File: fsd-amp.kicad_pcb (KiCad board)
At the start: 2 copper layers, 13 parts, among them J1001 Screw_Terminal_01x06, J1004 AudioJack2_Ground_Switch, Q1001 FZT 653 ZET, Q1002 FZT 653 ZET, Q1003 FZT 753 ZET

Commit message: define edge cuts board outline
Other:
- board outline added: 100 x 75 mm
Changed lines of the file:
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@@
 		)
 	)
+	(gr_rect
+		(start 100 50)
+		(end 200 125)
+		(stroke
+			(width 0.05)
+			(type default)
+		)
+		(fill none)
+		(layer "Edge.Cuts")
+	)
 )

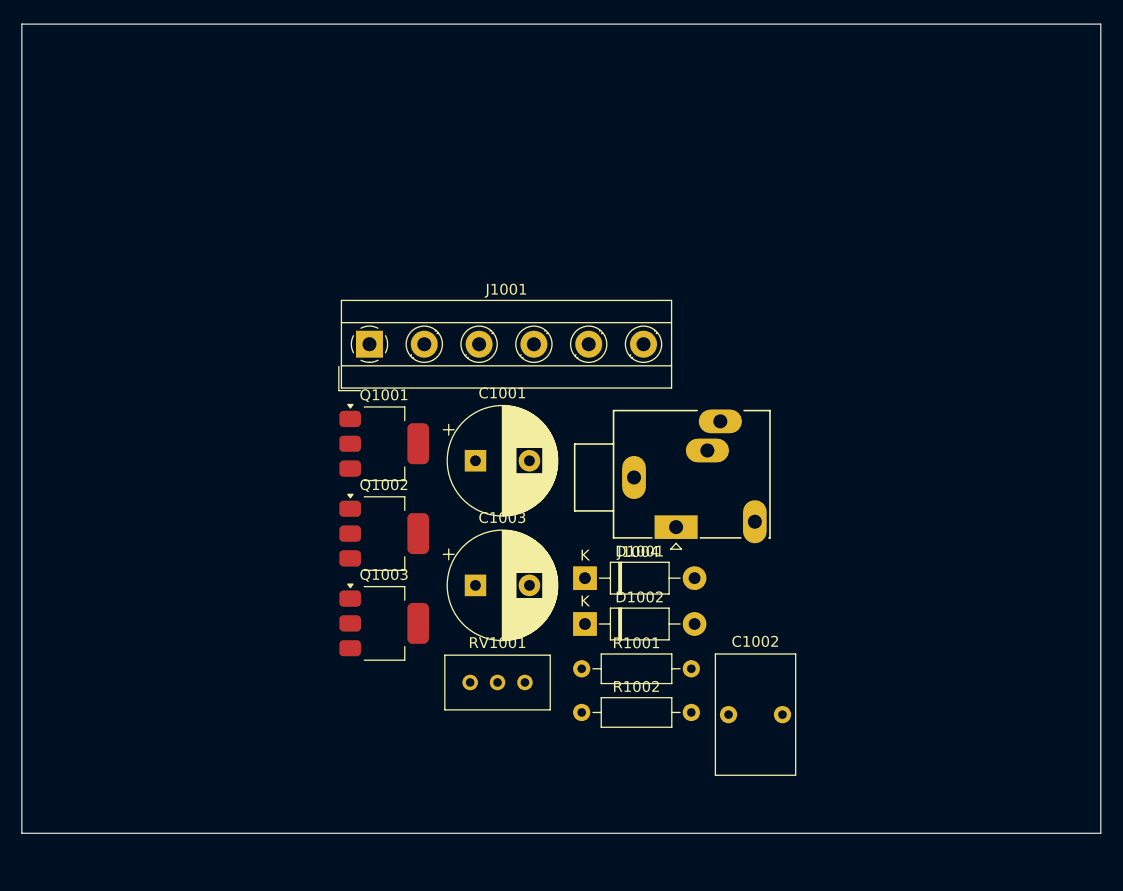
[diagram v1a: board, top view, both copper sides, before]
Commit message: coarse placement of footprints
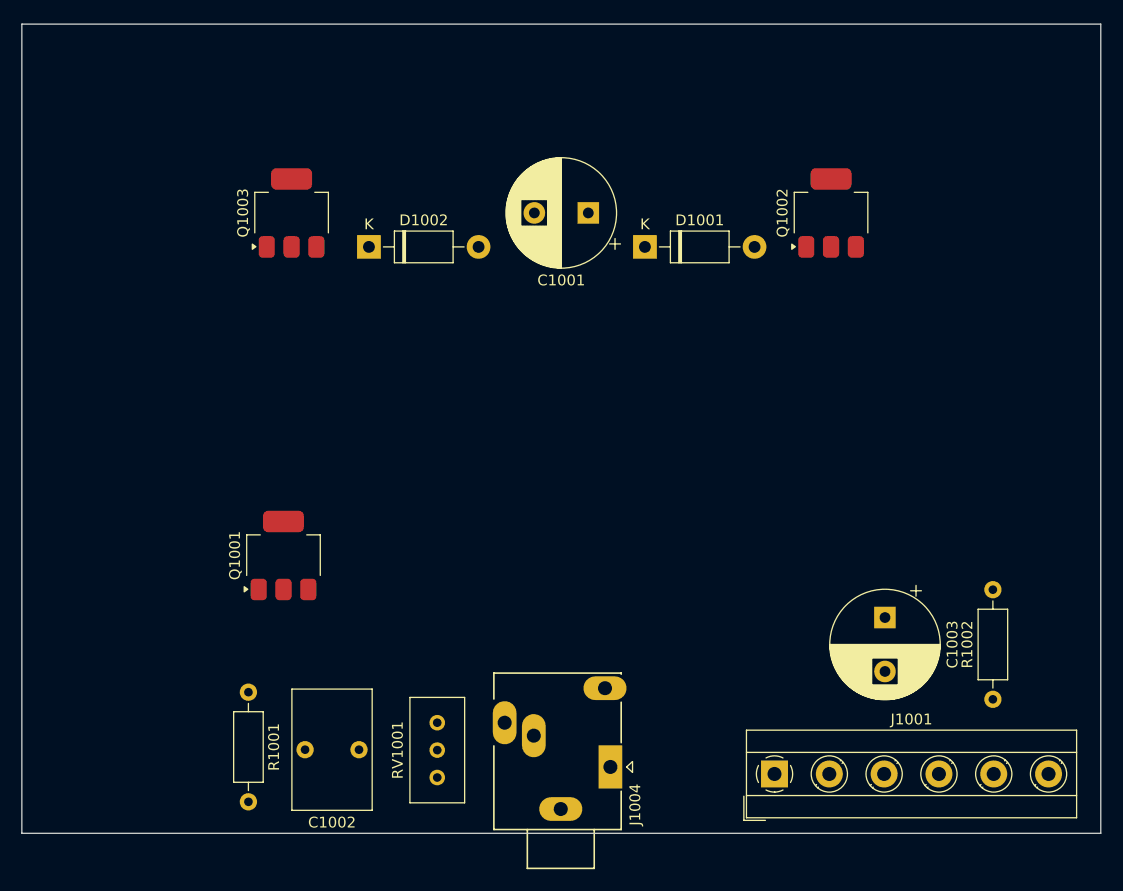
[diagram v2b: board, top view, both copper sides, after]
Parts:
- moved J1001 54.7 mm to (169.8, 119.5)
- moved Q1002 51.0 mm to (175.0, 67.5), turned to 90 degrees
- moved D1002 40.3 mm to (132.2, 70.7)
- moved Q1003 39.0 mm to (125.0, 67.5), turned to 90 degrees
- moved R1002 38.1 mm to (190.0, 112.6), turned to 90 degrees
- moved C1003 38.1 mm to (180.0, 105.0), turned to -90 degrees
- moved C1002 34.4 mm to (131.2, 117.2), turned to 180 degrees
- moved D1001 31.2 mm to (157.8, 70.7)
- moved R1001 31.0 mm to (121.0, 111.9), turned to -90 degrees
- moved C1001 25.2 mm to (152.5, 67.5), turned to 180 degrees
- moved J1004 23.0 mm to (154.6, 118.8), turned to 90 degrees
- moved Q1001 13.9 mm to (124.2, 99.2), turned to 90 degrees
- moved RV1001 8.94 mm to (138.5, 114.8), turned to 90 degrees

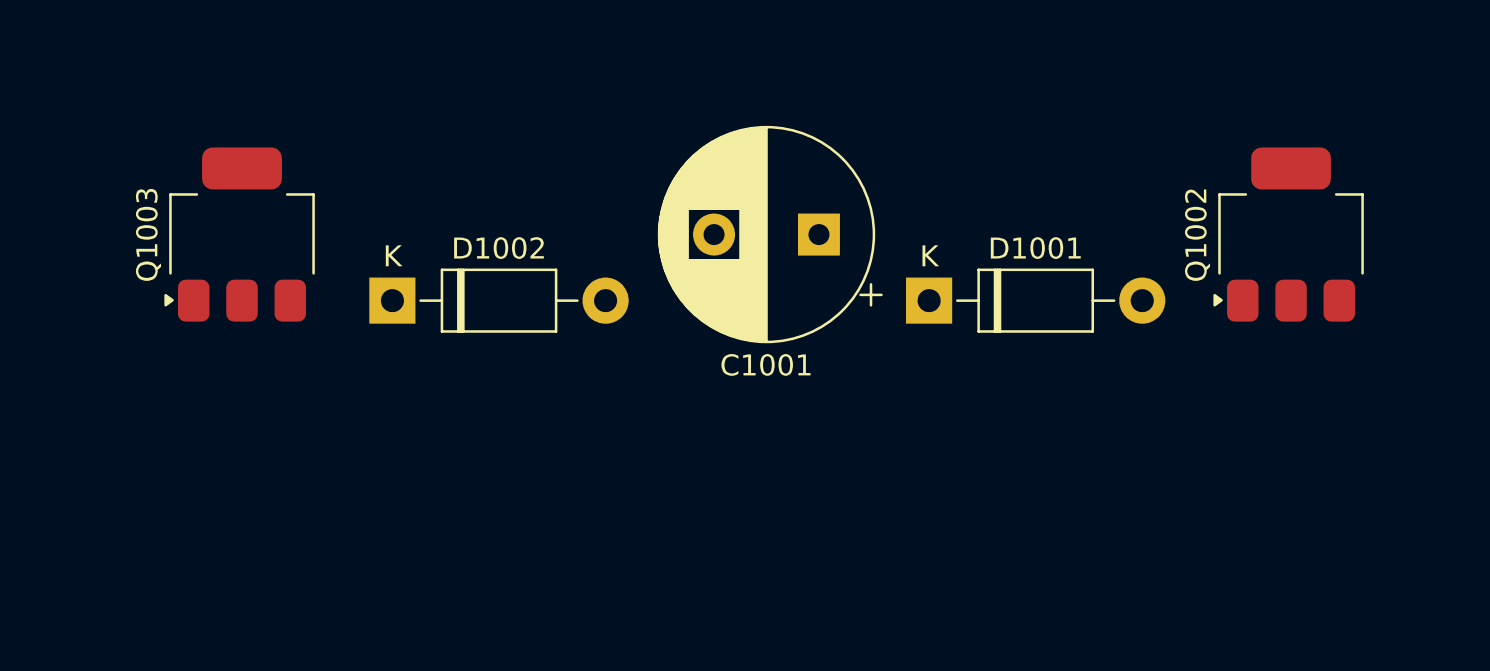
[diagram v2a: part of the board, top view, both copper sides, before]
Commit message: fix placement of power bjt
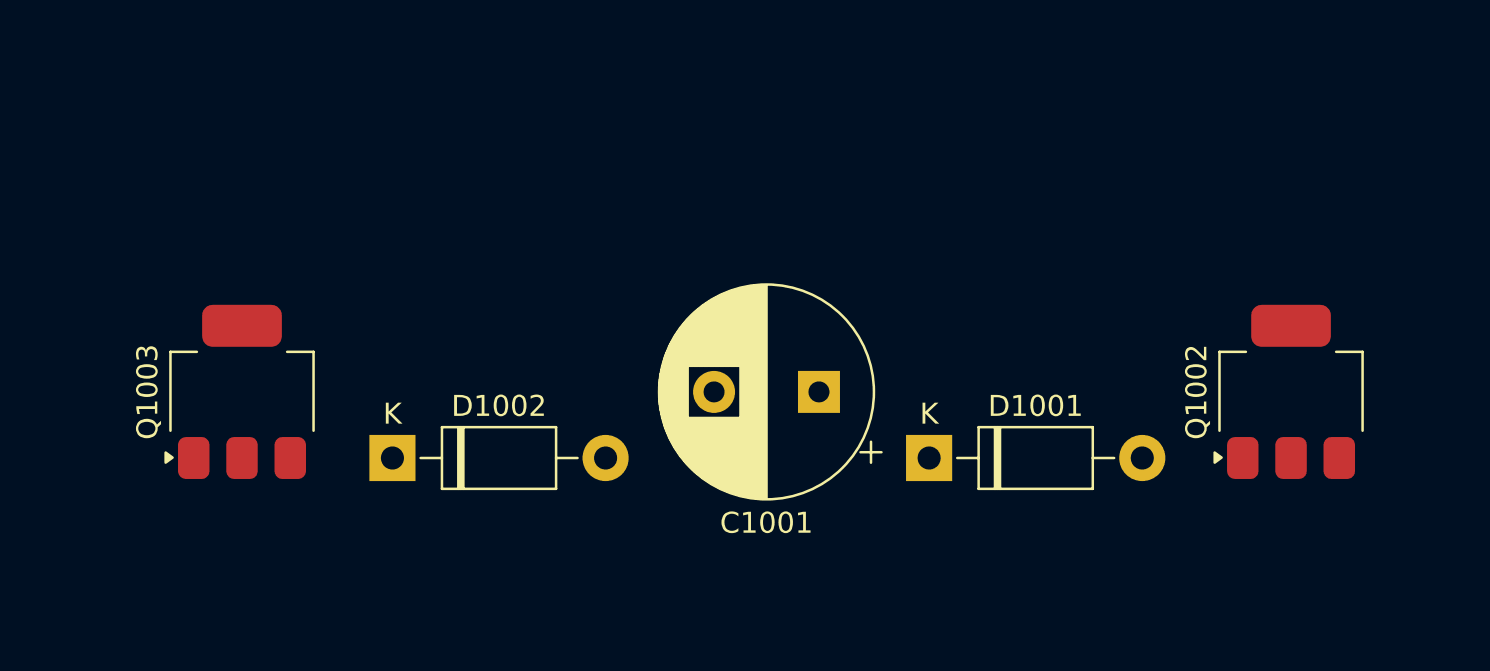
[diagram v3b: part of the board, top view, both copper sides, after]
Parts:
- moved C1001 7.50 mm to (152.5, 75.0)
- moved D1001 7.50 mm to (157.8, 78.2)
- moved D1002 7.50 mm to (132.2, 78.2)
- moved Q1002 7.50 mm to (175.0, 75.0)
- moved Q1003 7.50 mm to (125.0, 75.0)
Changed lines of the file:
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@@
 		(tags "Potentiometer vertical Bourns 3296W")
 		(property "Reference" "RV1001"
-			(at -2.54 -3.66 270)
+			(at -2.54 -3.66 -90)
 			(layer "F.SilkS")
 			(effects
@@
 		)
 		(property "Value" "20k"
-			(at -2.54 3.67 270)
+			(at -2.54 3.67 -90)
 			(layer "F.Fab")
 			(effects
@@
 		)
 		(fp_text user "${REFERENCE}"
-			(at -3.175 0.005 270)
+			(at -3.175 0.005 -90)
 			(layer "F.Fab")
 			(effects
@@
 	(footprint "fp:CP_Radial_D10.0mm_P5.00mm"
 		(layer "F.Cu")
-		(at 152.5 67.5 180)
+		(at 152.5 75 180)
 		(descr "CP, Radial series, Radial, pin pitch=5.00mm, , diameter=10mm, Electrolytic Capacitor")
 		(tags "CP Radial series Radial pin pitch 5.00mm  diameter 10mm Electrolytic Capacitor")
@@
 		(tags "Resistor Axial_DIN0207 series Axial Horizontal pin pitch 10.16mm 0.25W = 1/4W length 6.3mm diameter 2.5mm")
 		(property "Reference" "R1002"
-			(at 5.08 -2.37 270)
+			(at 5.08 -2.37 -90)
 			(layer "F.SilkS")
 			(effects
@@
 		)
 		(property "Value" "150"
-			(at 5.08 2.37 270)
+			(at 5.08 2.37 -90)
 			(layer "F.Fab")
 			(effects
@@
 		)
 		(fp_text user "${REFERENCE}"
-			(at 5.08 0 270)
+			(at 5.08 0 -90)
 			(layer "F.Fab")
 			(effects
@@
 		(tags "jack stereo TRS")
 		(property "Reference" "J1004"
-			(at -3.5 2.3 270)
+			(at -3.5 2.3 -90)
 			(layer "F.SilkS")
 			(effects
@@
 		)
 		(property "Value" "AudioJack2_Ground_Switch"
-			(at 2.3 -12.2 270)
+			(at 2.3 -12.2 -90)
 			(layer "F.Fab")
 			(effects
@@
 		)
 		(fp_text user "${REFERENCE}"
-			(at 2.7 -4.6 270)
+			(at 2.7 -4.6 -90)
 			(layer "F.Fab")
 			(effects
@@
 		(tags "CMS SOT")
 		(property "Reference" "Q1001"
-			(at 0 -4.5 270)
+			(at 0 -4.5 -90)
 			(layer "F.SilkS")
 			(effects
@@
 		)
 		(property "Value" "FZT 653 ZET"
-			(at 0 4.5 270)
+			(at 0 4.5 -90)
 			(layer "F.Fab")
 			(effects
@@
 		)
 		(fp_text user "${REFERENCE}"
-			(at 0 0 360)
+			(at 0 0 0)
 			(layer "F.Fab")
 			(effects
@@
 	(footprint "fp:SOT-223-3_TabPin2"
 		(layer "F.Cu")
-		(at 175 67.5 90)
+		(at 175 75 90)
 		(descr "module CMS SOT223 4 pins")
 		(tags "CMS SOT")
 		(property "Reference" "Q1002"
-			(at 0 -4.5 270)
+			(at 0 -4.5 -90)
 			(layer "F.SilkS")
 			(effects
@@
 		)
 		(property "Value" "FZT 653 ZET"
-			(at 0 4.5 270)
+			(at 0 4.5 -90)
 			(layer "F.Fab")
 			(effects
@@
 		)
 		(fp_text user "${REFERENCE}"
-			(at 0 0 360)
+			(at 0 0 0)
 			(layer "F.Fab")
 			(effects
@@
 	(footprint "fp:SOT-223-3_TabPin2"
 		(layer "F.Cu")
-		(at 125 67.5 90)
+		(at 125 75 90)
 		(descr "module CMS SOT223 4 pins")
 		(tags "CMS SOT")
 		(property "Reference" "Q1003"
-			(at 0 -4.5 270)
+			(at 0 -4.5 -90)
 			(layer "F.SilkS")
 			(effects
@@
 		)
 		(property "Value" "FZT 753 ZET"
-			(at 0 4.5 270)
+			(at 0 4.5 -90)
 			(layer "F.Fab")
 			(effects
@@
 		)
 		(fp_text user "${REFERENCE}"
-			(at 0 0 360)
+			(at 0 0 0)
 			(layer "F.Fab")
 			(effects
@@
 	(footprint "fp:D_DO-41_SOD81_P10.16mm_Horizontal"
 		(layer "F.Cu")
-		(at 132.17 70.65)
+		(at 132.17 78.15)
 		(descr "Diode, DO-41_SOD81 series, Axial, Horizontal, pin pitch=10.16mm, , length*diameter=5.2*2.7mm^2, , http://www.diodes.com/_files/packages/DO-41%20(Plastic).pdf")
 		(tags "Diode DO-41_SOD81 series Axial Horizontal pin pitch 10.16mm  length 5.2mm diameter 2.7mm")
 		(property "Reference" "D1002"
-			(at 5.08 -2.47 360)
+			(at 5.08 -2.47 0)
 			(layer "F.SilkS")
 			(effects
@@
 		)
 		(property "Value" "1N4001"
-			(at 5.08 2.47 360)
+			(at 5.08 2.47 0)
 			(layer "F.Fab")
 			(effects
@@
 		)
 		(fp_text user "K"
-			(at 0 -2.1 360)
+			(at 0 -2.1 0)
 			(layer "F.SilkS")
 			(effects
@@
 		)
 		(fp_text user "${REFERENCE}"
-			(at 5.47 0 360)
+			(at 5.47 0 0)
 			(layer "F.Fab")
 			(effects
@@
 		)
 		(fp_text user "K"
-			(at 0 -2.1 360)
+			(at 0 -2.1 0)
 			(layer "F.Fab")
 			(effects
@@
 	(footprint "fp:D_DO-41_SOD81_P10.16mm_Horizontal"
 		(layer "F.Cu")
-		(at 157.75 70.65)
+		(at 157.75 78.15)
 		(descr "Diode, DO-41_SOD81 series, Axial, Horizontal, pin pitch=10.16mm, , length*diameter=5.2*2.7mm^2, , http://www.diodes.com/_files/packages/DO-41%20(Plastic).pdf")
 		(tags "Diode DO-41_SOD81 series Axial Horizontal pin pitch 10.16mm  length 5.2mm diameter 2.7mm")
 		(property "Reference" "D1001"
-			(at 5.08 -2.47 360)
+			(at 5.08 -2.47 0)
 			(layer "F.SilkS")
 			(effects
@@
 		)
 		(property "Value" "1N4001"
-			(at 5.08 2.47 360)
+			(at 5.08 2.47 0)
 			(layer "F.Fab")
 			(effects
@@
 		)
 		(fp_text user "K"
-			(at 0 -2.1 360)
+			(at 0 -2.1 0)
 			(layer "F.SilkS")
 			(effects
@@
 		)
 		(fp_text user "K"
-			(at 0 -2.1 360)
+			(at 0 -2.1 0)
 			(layer "F.Fab")
 			(effects
@@
 		)
 		(fp_text user "${REFERENCE}"
-			(at 5.47 0 360)
+			(at 5.47 0 0)
 			(layer "F.Fab")
 			(effects

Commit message: add routing
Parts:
- added REF**: MountingHole_3.2mm_M3_Pad_Via, MountingHole:MountingHole_3.2mm_M3_Pad_Via, F.Cu at (105.0, 55.0)
- added REF**: MountingHole_3.2mm_M3_Pad_Via, MountingHole:MountingHole_3.2mm_M3_Pad_Via, F.Cu at (195.0, 55.0)
- added REF**: MountingHole_3.2mm_M3_Pad_Via, MountingHole:MountingHole_3.2mm_M3_Pad_Via, F.Cu at (195.0, 105.0)
- added REF**: MountingHole_3.2mm_M3_Pad_Via, MountingHole:MountingHole_3.2mm_M3_Pad_Via, F.Cu at (105.0, 105.0)
- moved C1003 36.0 mm to (150.0, 85.1)
- moved R1001 29.8 mm to (122.8, 82.2)
- moved R1002 26.6 mm to (172.8, 92.3)
- moved J1001 23.4 mm to (157.9, 99.2)
- moved C1002 18.4 mm to (133.6, 99.0), turned to 90 degrees
- moved J1004 15.2 mm to (151.8, 103.8)
- moved RV1001 10.0 mm to (136.1, 105.0), turned to 0 degrees
- moved Q1001 4.04 mm to (120.5, 100.8), turned to -90 degrees
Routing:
- net GND: track 0.00 -> 78.2 mm
- net Net-(Q1002-E): track 0.00 -> 60.7 mm
- net Net-(D1002-K): track 0.00 -> 38.5 mm
- net /amp_in: track 0.00 -> 35.9 mm
- net /amp_out: track 0.00 -> 24.6 mm
- net Net-(Q1001-B): track 0.00 -> 16.8 mm
- net Net-(D1001-K): track 0.00 -> 15.4 mm
- net Net-(C1002-Pad1): track 0.00 -> 6.02 mm
- net Net-(D1001-A): track 0.00 -> 4.79 mm
- added copper zone on F.Cu, net +9V
- added copper zone on F.Cu, net GND
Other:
- board size 100 x 75 mm -> 100 x 60 mm
